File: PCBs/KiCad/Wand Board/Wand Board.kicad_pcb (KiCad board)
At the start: 2 copper layers, 86 x 56 mm, 25 parts, among them J1 BRL LEDS, J10 ENC BTN, J11 ENCODER, J12 POW_IN, J13 BRL SENSE, J14 BAR, J15 DISP, J16 USB DATA, J2 BODY LEDS, J3 TIP LED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

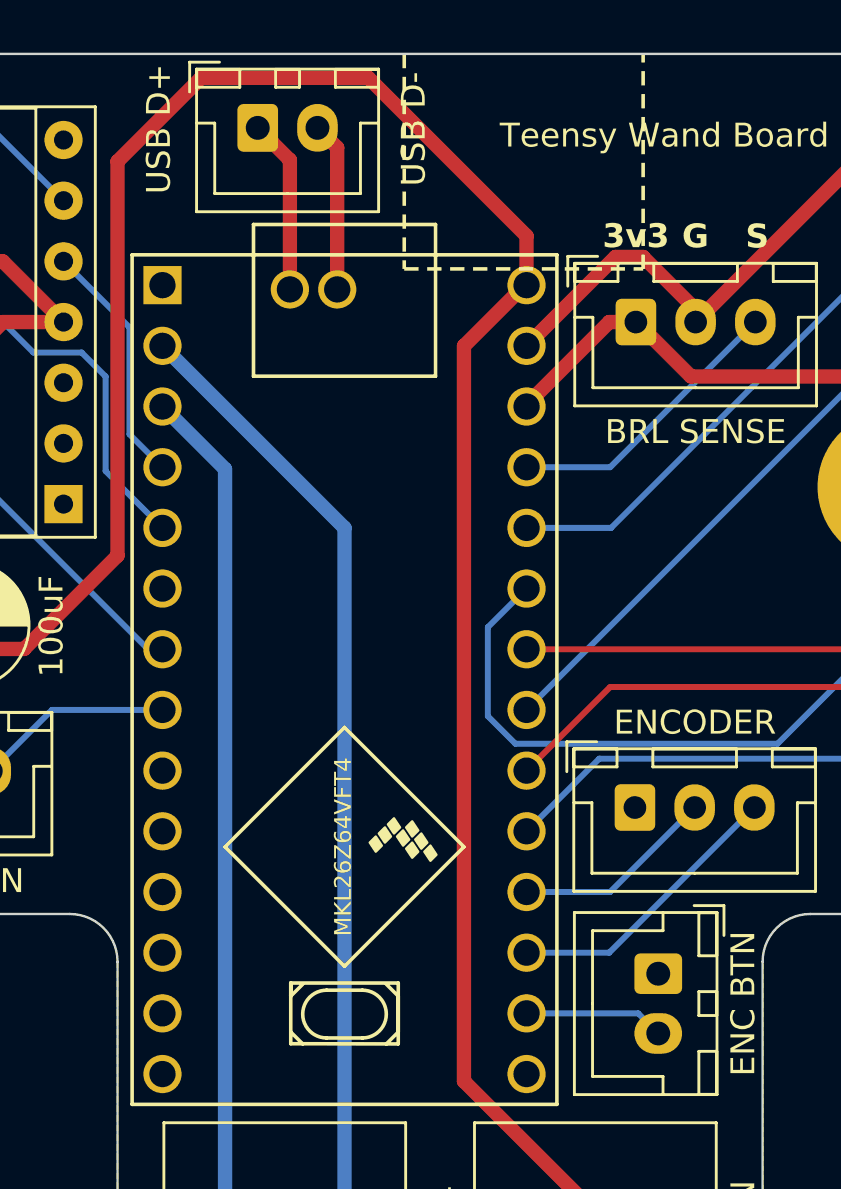
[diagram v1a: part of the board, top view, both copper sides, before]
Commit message: Updated Wand Board PCB: Migrate to Teensy 4.0, Change Encoder Pin Order
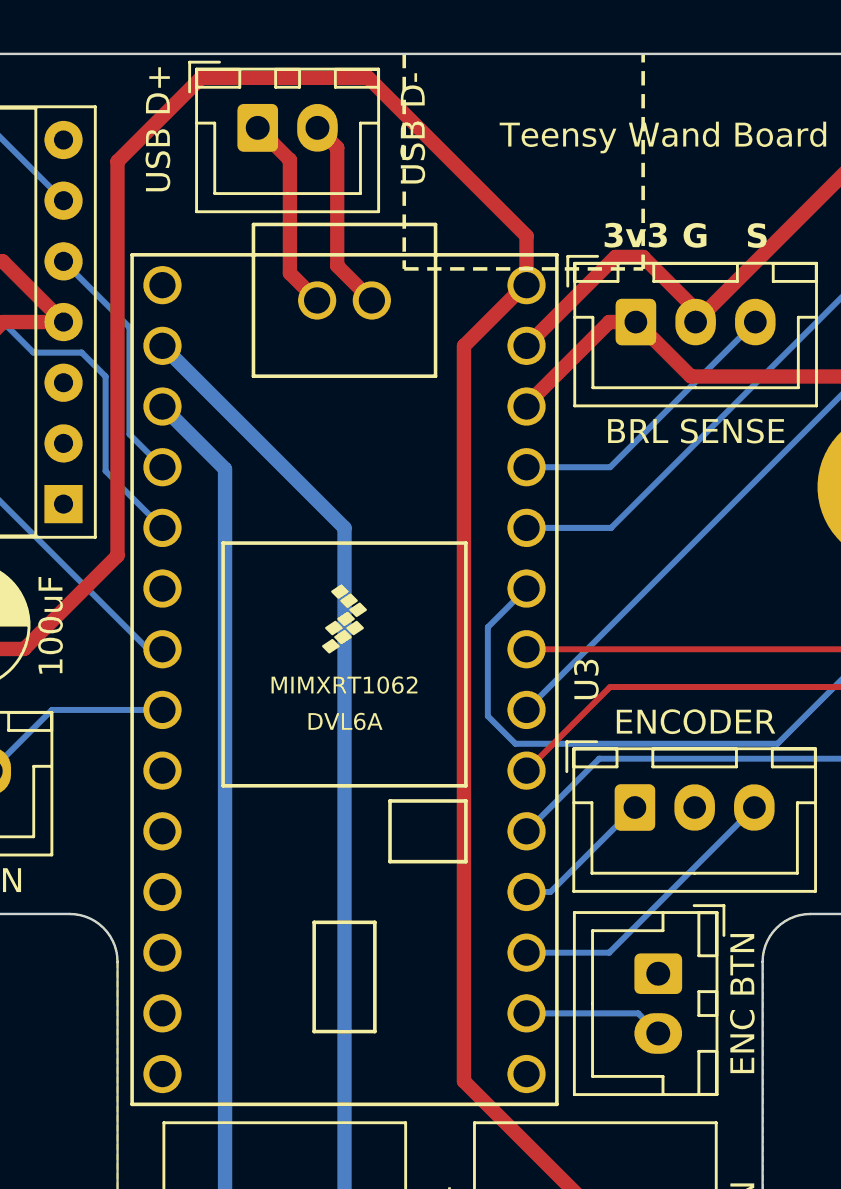
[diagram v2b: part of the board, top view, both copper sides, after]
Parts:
- removed U2: Teensy-LC, Teensy:Teensy_LC
- added U3: Teensy4.0, Teensy:Teensy40-DHolesOnly, F.Cu at (90.5, 92.7)
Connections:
- J11 pad 1: GND -> Net-(J11-Pin_1)
- J11 pad 2: Net-(J11-Pin_2) -> GND
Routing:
- net Net-(J11-Pin_2): track 8.50 -> 0.00 mm
- net Net-(J11-Pin_1): track 0.00 -> 6.00 mm
- net /D-: track 7.10 -> 8.17 mm
- net /D+: track 7.32 -> 8.25 mm

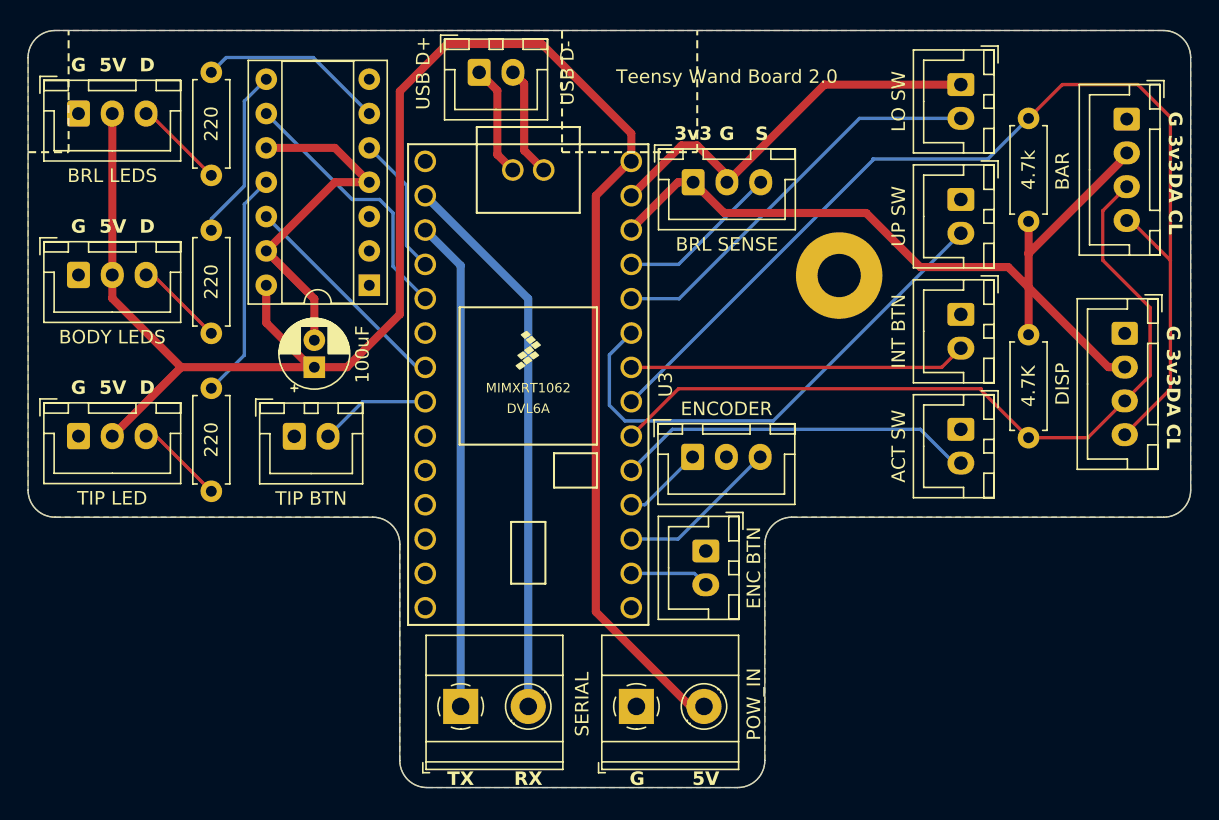
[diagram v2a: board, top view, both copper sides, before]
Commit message: Added motor output for wand rumble
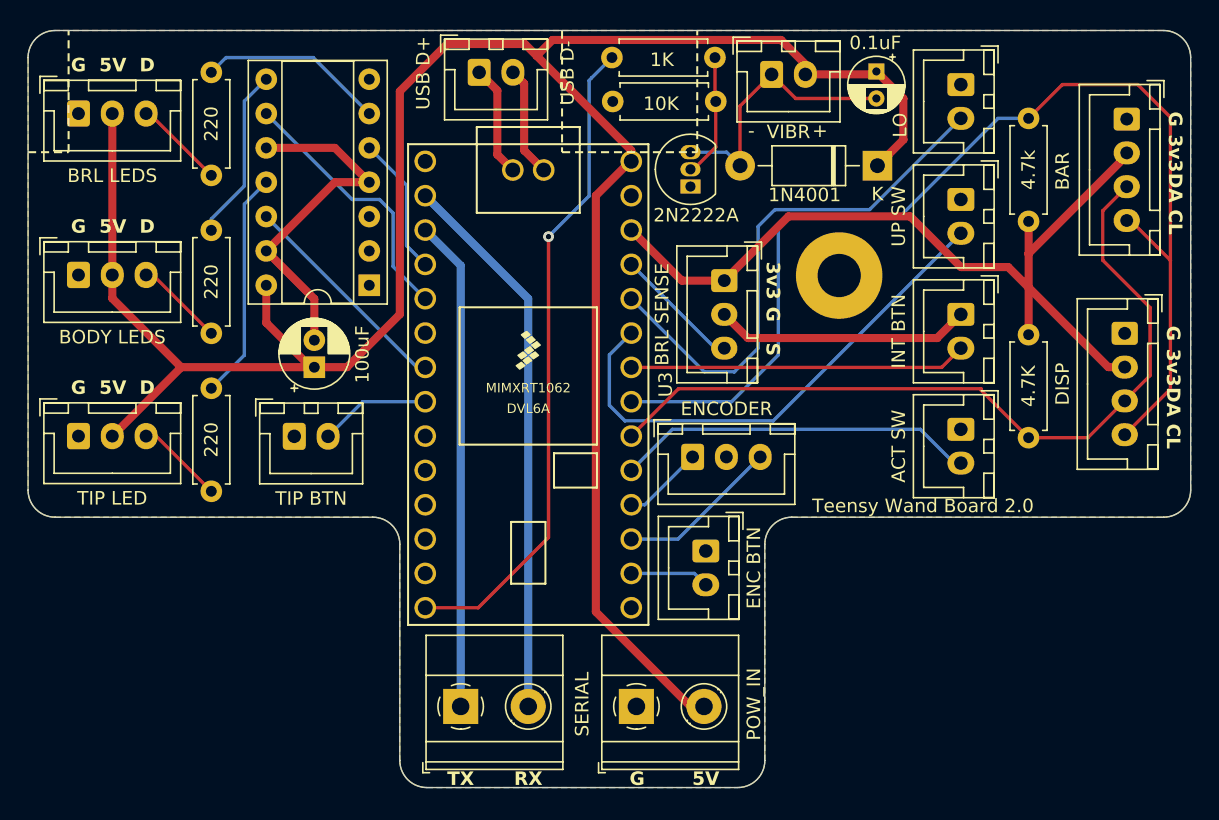
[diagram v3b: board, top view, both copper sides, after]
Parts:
- added C2: 0.1uF, Capacitor_THT:CP_Radial_D4.0mm_P2.00mm, F.Cu at (116.2, 69.5)
- added D1: 1N4001, Diode_THT:D_DO-41_SOD81_P10.16mm_Horizontal, F.Cu at (116.3, 76.5)
- added J17: VIBR, Connector_JST:JST_XH_B2B-XH-A_1x02_P2.50mm_Vertical, F.Cu at (108.5, 69.8)
- added Q1: 2N2222A, Package_TO_SOT_THT:TO-92_Inline, F.Cu at (102.5, 78.0)
- added R6: 10k, Resistor_THT:R_Axial_DIN0207_L6.3mm_D2.5mm_P7.62mm_Horizontal, F.Cu at (104.4, 71.8)
- added R7: 1k, Resistor_THT:R_Axial_DIN0207_L6.3mm_D2.5mm_P7.62mm_Horizontal, F.Cu at (104.3, 68.5)
- J8: value LO SW -> LO
- moved J13 7.63 mm to (105.0, 85.0), turned to -90 degrees
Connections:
- U3 pad 14: unconnected-(U3-12_MISO_MQSL-Pad14) -> Net-(U3-12_MISO_MQSL)
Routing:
- net Net-(U3-12_MISO_MQSL): track 0.00 -> 48.7 mm, vias 0 -> 1
- net +5V: track 138.7 -> 173.8 mm
- net /MOT-: track 0.00 -> 20.3 mm
- net GND: track 56.8 -> 45.4 mm
- net Net-(J8-Pin_2): track 29.9 -> 39.7 mm
- net Net-(Q1-B): track 0.00 -> 9.20 mm
- net /SCL: track 80.0 -> 85.5 mm
- net Net-(J13-Pin_3): track 12.1 -> 9.45 mm
- net +3.3V: track 62.5 -> 63.5 mm
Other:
- board text added: "+"
- board text added: "-"
- board text added: "0.1uF"
- board text added: "10K"
- board text added: "1K"
- board text added: "1N4001"
- board text added: "2N2222A"
- board text added: "JLCJLCJLCJLC"

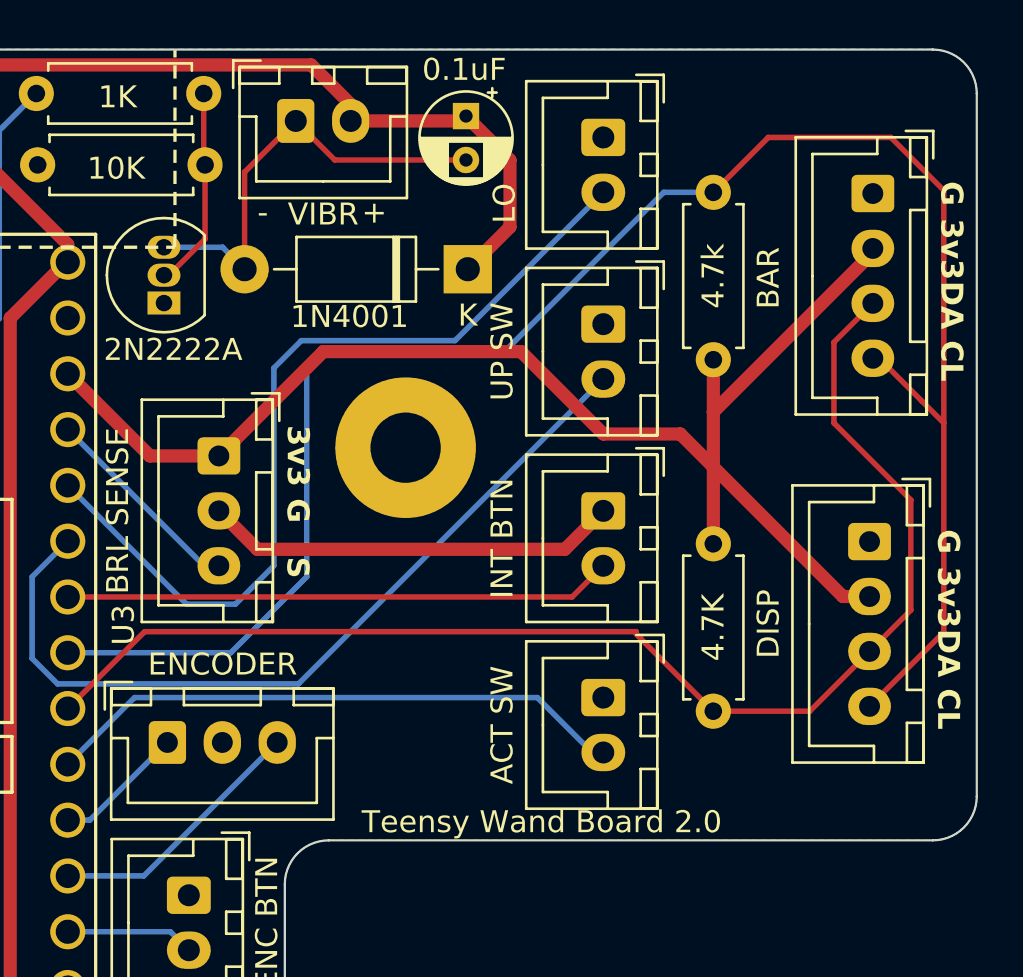
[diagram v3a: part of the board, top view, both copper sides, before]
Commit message: Added additional i2c output to wand board for optional driver
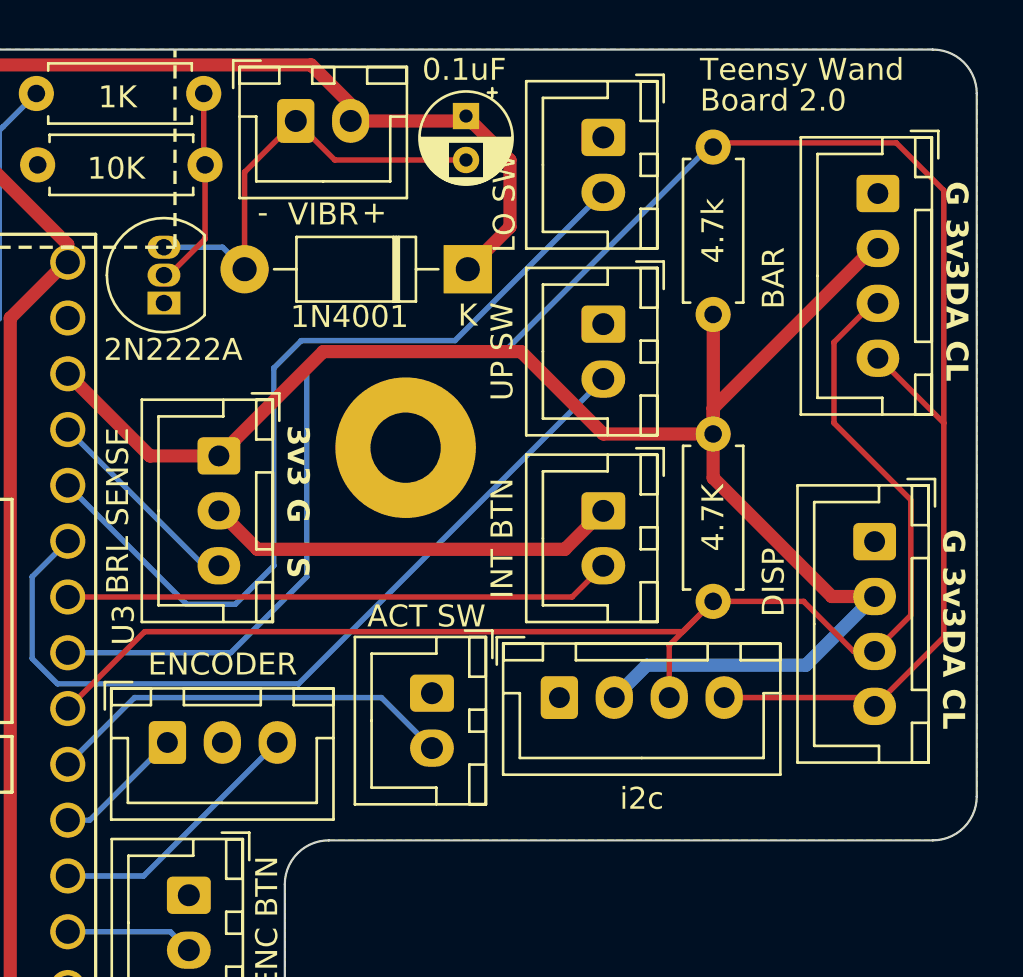
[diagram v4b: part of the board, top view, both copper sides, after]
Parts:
- added J18: i2c, Connector_JST:JST_XH_B4B-XH-A_1x04_P2.50mm_Vertical, F.Cu at (120.5, 96.0)
- J8: value LO -> LO SW
- moved J6 7.80 mm to (114.7, 95.8)
- moved R4 5.00 mm to (127.5, 91.6)
- moved R5 2.06 mm to (127.5, 70.9)
- moved J14 0.23 mm to (134.8, 73.2)
- moved J15 0.23 mm to (134.8, 88.9)
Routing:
- net +3.3V: track 63.5 -> 76.7 mm
- net Net-(J6-Pin_2): track 26.7 -> 19.2 mm
- net /SCL: track 85.5 -> 92.4 mm
- net /SDA: track 59.4 -> 63.6 mm
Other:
- board text added: "Board 2.0"
- board text added: "Teensy Wand"
- board text removed: "Teensy Wand Board 2.0"

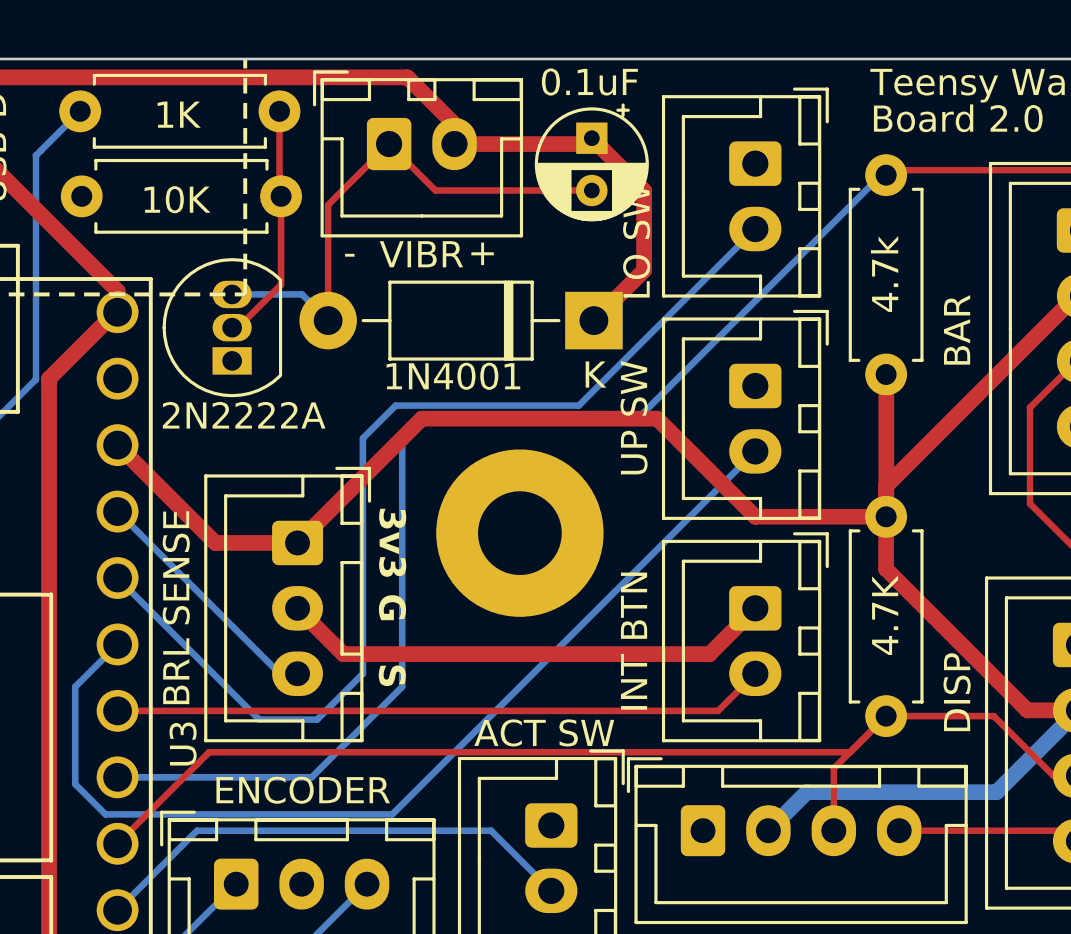
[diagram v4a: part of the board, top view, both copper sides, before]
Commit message: Fixed Gerbers for extended i2c wand board.  Exported STEP files of boards for jig creation.
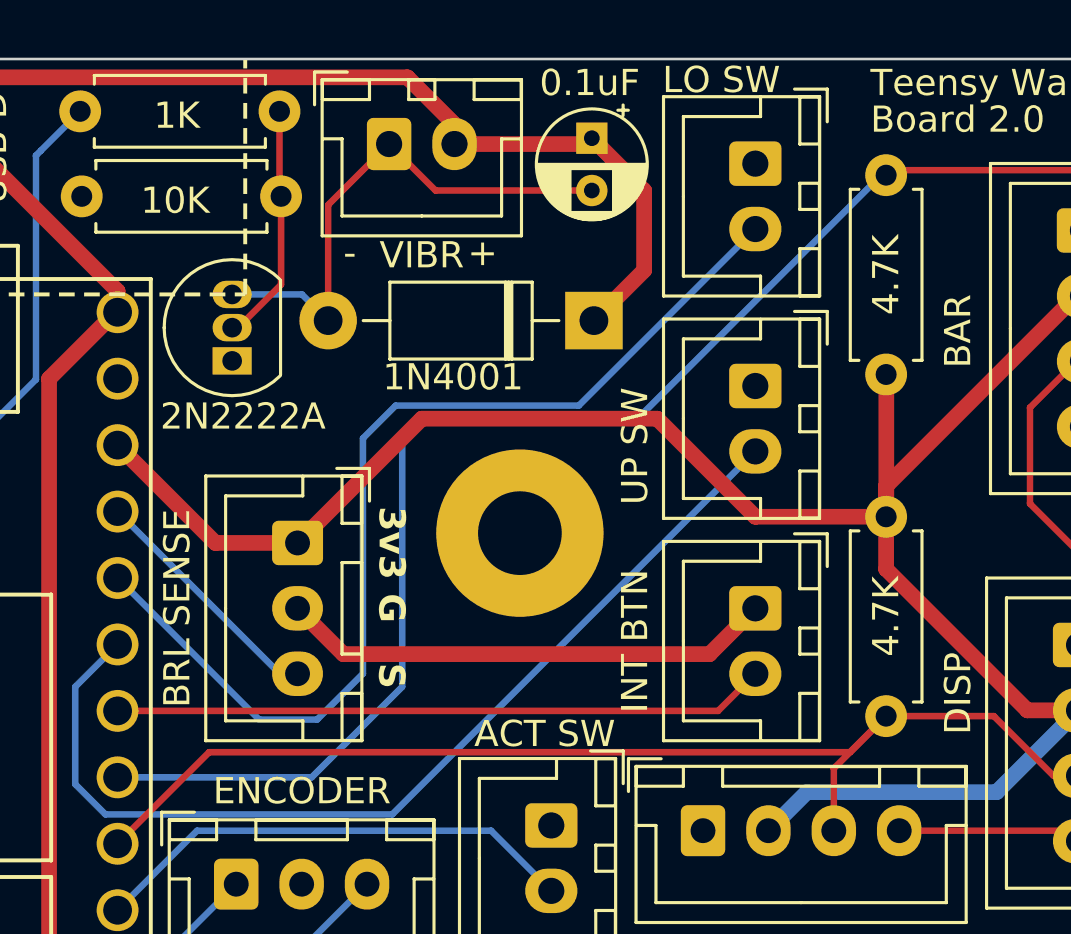
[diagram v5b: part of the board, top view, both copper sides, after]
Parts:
- R5: value 4.7k -> 4.7K
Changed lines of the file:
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@@
     (property "Sheetname" "")
     (attr through_hole)
-    (fp_text reference "U3" (at 0 -10.16 90) (layer "F.SilkS")
+    (fp_text reference "U3" (at 0 -10.16 90) (layer "F.SilkS") hide
         (effects (font (size 1 1) (thickness 0.15)))
     )
@@
         (effects (font (size 1 1) (thickness 0.15)))
     )
-    (fp_text value "4.7k" (at 3.81 0 90) (layer "F.SilkS")
+    (fp_text value "4.7K" (at 3.81 0 90) (layer "F.SilkS")
         (effects (font (size 1 1) (thickness 0.15)))
     )
@@
         (effects (font (size 1 1) (thickness 0.15)))
     )
-    (fp_text user "K" (at 0 -2.1) (layer "F.SilkS")
+    (fp_text user "K" (at 0 -2.1) (layer "F.SilkS") hide
         (effects (font (size 1 1) (thickness 0.15)))
     )
@@
         (effects (font (size 1 1) (thickness 0.15)))
     )
-    (fp_text value "UP SW" (at 1.25 4.6 90) (layer "F.SilkS")
+    (fp_text value "UP SW" (at 2.3 4.6 90) (layer "F.SilkS")
         (effects (font (size 1 1) (thickness 0.15)))
     )
@@
         (effects (font (size 1 1) (thickness 0.15)))
     )
-    (fp_text value "LO SW" (at 3 4.5 90) (layer "F.SilkS")
-        (effects (font (size 1 1) (thickness 0.15)))
-    )
+    (fp_text value "LO SW" (at -3.2 1.3 -180) (layer "F.SilkS")
+        (effects (font (size 1 1) (thickness 0.15)))
+    )
